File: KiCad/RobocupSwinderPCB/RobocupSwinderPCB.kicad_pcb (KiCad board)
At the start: 2 copper layers, 92 x 57 mm, 30 parts, among them J1 Barrel_Jack, M1 Stepper_Motor_bipolar, M2 Stepper_Motor_bipolar, SW1 Limit_Switch, SW2 Limit_Switch, SW3 SW_SPST, U1 Teensy4.1, U3 LM7805_TO220

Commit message: Pcb cleanup
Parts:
- U1: footprint TeensyLibrary:Teensy41-Pins-Only_Silkscreen -> SwinderFootprintLibrary:Teensy41-Pins-Only_Silkscreen
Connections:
- LCD1 pad 3: /LCD_SDA_Pin_18 -> /LCD_SCL_Pin_19
- LCD1 pad 4: /LCD_SCL_Pin_19 -> /LCD_SDA_Pin_18
- RE1 pad 3: /RE_SW_Pin_21 -> /RE_CLK_Pin_23
- RE1 pad 5: /RE_CLK_Pin_23 -> /RE_SW_Pin_21
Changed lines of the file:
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@@
 		)
 		(property ki_fp_filters "SW*DPDT*")
-		(sheetname "Root")
+		(sheetname "/")
 		(sheetfile "RobocupSwinderPCB.kicad_sch")
 		(attr through_hole)
@@
 		)
 		(property ki_fp_filters "R_*")
-		(sheetname "Root")
+		(sheetname "/")
 		(sheetfile "RobocupSwinderPCB.kicad_sch")
 		(attr smd)
@@
 		)
 		(property ki_fp_filters "CP_*")
-		(sheetname "Root")
+		(sheetname "/")
 		(sheetfile "RobocupSwinderPCB.kicad_sch")
 		(attr through_hole)
@@
 		)
 		(property ki_fp_filters "SW*DPDT*")
-		(sheetname "Root")
+		(sheetname "/")
 		(sheetfile "RobocupSwinderPCB.kicad_sch")
 		(attr through_hole)
@@
 		)
 		(property ki_fp_filters "LED* LED_SMD:* LED_THT:*")
-		(sheetname "Root")
+		(sheetname "/")
 		(sheetfile "RobocupSwinderPCB.kicad_sch")
 		(attr smd)
@@
 		)
 		(property ki_fp_filters "MountingHole*Pad*")
-		(sheetname "Root")
+		(sheetname "/")
 		(sheetfile "RobocupSwinderPCB.kicad_sch")
 		(attr exclude_from_pos_files exclude_from_bom)
@@
 		)
 		(property ki_fp_filters "R_*")
-		(sheetname "Root")
+		(sheetname "/")
 		(sheetfile "RobocupSwinderPCB.kicad_sch")
 		(attr smd)
@@
 			)
 		)
-		(sheetname "Root")
+		(sheetname "/")
 		(sheetfile "RobocupSwinderPCB.kicad_sch")
 		(attr through_hole)
@@
 			(layers "*.Cu" "*.Mask")
 			(remove_unused_layers no)
-			(net 25 "/LCD_SDA_Pin_18")
+			(net 26 "/LCD_SCL_Pin_19")
 			(pinfunction "SDA")
 			(pintype "bidirectional")
@@
 			(layers "*.Cu" "*.Mask")
 			(remove_unused_layers no)
-			(net 26 "/LCD_SCL_Pin_19")
+			(net 25 "/LCD_SDA_Pin_18")
 			(pinfunction "SCL")
 			(pintype "bidirectional")
@@
 		)
 		(property ki_fp_filters "MountingHole*Pad*")
-		(sheetname "Root")
+		(sheetname "/")
 		(sheetfile "RobocupSwinderPCB.kicad_sch")
 		(attr exclude_from_pos_files exclude_from_bom)
@@
 			)
 		)
-		(sheetname "Root")
+		(sheetname "/")
 		(sheetfile "RobocupSwinderPCB.kicad_sch")
 		(attr through_hole)
@@
 		)
 	)
-	(footprint "TeensyLibrary:Teensy41-Pins-Only_Silkscreen"
+	(footprint "SwinderFootprintLibrary:Teensy41-Pins-Only_Silkscreen"
 		(layer "F.Cu")
 		(at 133.01 104.37)
 		(property "Reference" "U1"
-			(at 0.07 9.98 0)
+			(at 0 -10.16 0)
 			(layer "F.SilkS")
 			(effects
@@
 			)
 		)
-		(sheetname "Root")
+		(sheetname "/")
 		(sheetfile "RobocupSwinderPCB.kicad_sch")
 		(attr through_hole)
@@
 			(effects
 				(font
-					(size 0.8 0.8)
+					(size 0.7 0.7)
 					(thickness 0.15)
 				)
@@
 			(effects
 				(font
-					(size 0.8 0.8)
+					(size 0.7 0.7)
 					(thickness 0.15)
 				)
@@
 		)
 		(property ki_fp_filters "Pololu*Breakout*15.2x20.3mm*")
-		(sheetname "Root")
+		(sheetname "/")
 		(sheetfile "RobocupSwinderPCB.kicad_sch")
 		(attr through_hole)
@@
 		)
 		(property ki_fp_filters "BarrelJack*")
-		(sheetname "Root")
+		(sheetname "/")
 		(sheetfile "RobocupSwinderPCB.kicad_sch")
 		(attr through_hole)
@@
 		)
 		(property ki_fp_filters "Choke_* *Coil* Inductor_* L_*")
-		(sheetname "Root")
+		(sheetname "/")
 		(sheetfile "RobocupSwinderPCB.kicad_sch")
 		(attr smd)
@@
 		)
 		(property ki_fp_filters "PinHeader*P2.54mm*Vertical* TerminalBlock* Motor*")
-		(sheetname "Root")
+		(sheetname "/")
 		(sheetfile "RobocupSwinderPCB.kicad_sch")
 		(attr through_hole)
@@
 		)
 		(property ki_fp_filters "C_*")
-		(sheetname "Root")
+		(sheetname "/")
 		(sheetfile "RobocupSwinderPCB.kicad_sch")
 		(attr smd)
@@
 		)
 		(property ki_fp_filters "TO?220*")
-		(sheetname "Root")
+		(sheetname "/")
 		(sheetfile "RobocupSwinderPCB.kicad_sch")
 		(attr smd)
@@
 		)
 		(property ki_fp_filters "MountingHole*Pad*")
-		(sheetname "Root")
+		(sheetname "/")
 		(sheetfile "RobocupSwinderPCB.kicad_sch")
 		(attr exclude_from_pos_files exclude_from_bom)
@@
 		)
 		(property ki_fp_filters "CP_*")
-		(sheetname "Root")
+		(sheetname "/")
 		(sheetfile "RobocupSwinderPCB.kicad_sch")
 		(attr through_hole)
@@
 		)
 		(property ki_fp_filters "PinHeader*P2.54mm*Vertical* TerminalBlock* Motor*")
-		(sheetname "Root")
+		(sheetname "/")
 		(sheetfile "RobocupSwinderPCB.kicad_sch")
 		(attr through_hole)
@@
 			)
 		)
-		(sheetname "Root")
+		(sheetname "/")
 		(sheetfile "RobocupSwinderPCB.kicad_sch")
 		(attr through_hole)
@@
 			(layers "*.Cu" "*.Mask")
 			(remove_unused_layers no)
-			(net 29 "/RE_SW_Pin_21")
+			(net 31 "/RE_CLK_Pin_23")
 			(pinfunction "CLK")
 			(pintype "output")
@@
 			(layers "*.Cu" "*.Mask")
 			(remove_unused_layers no)
-			(net 31 "/RE_CLK_Pin_23")
+			(net 29 "/RE_SW_Pin_21")
 			(pinfunction "SW")
 			(pintype "output")
@@
 		)
 		(property ki_fp_filters "R_*")
-		(sheetname "Root")
+		(sheetname "/")
 		(sheetfile "RobocupSwinderPCB.kicad_sch")
 		(attr smd)
@@
 		)
 		(property ki_fp_filters "C_*")
-		(sheetname "Root")
+		(sheetname "/")
 		(sheetfile "RobocupSwinderPCB.kicad_sch")
 		(attr smd)
@@
 		)
 		(property ki_fp_filters "*Fuse*")
-		(sheetname "Root")
+		(sheetname "/")
 		(sheetfile "RobocupSwinderPCB.kicad_sch")
 		(attr smd)
@@
 		)
 		(property ki_fp_filters "C_*")
-		(sheetname "Root")
+		(sheetname "/")
 		(sheetfile "RobocupSwinderPCB.kicad_sch")
 		(attr smd)
@@
 		)
 		(property ki_fp_filters "R_*")
-		(sheetname "Root")
+		(sheetname "/")
 		(sheetfile "RobocupSwinderPCB.kicad_sch")
 		(attr smd)
@@
 		)
 		(property ki_fp_filters "LED* LED_SMD:* LED_THT:*")
-		(sheetname "Root")
+		(sheetname "/")
 		(sheetfile "RobocupSwinderPCB.kicad_sch")
 		(attr smd)
@@
 		)
 		(property ki_fp_filters "Pololu*Breakout*15.2x20.3mm*")
-		(sheetname "Root")
+		(sheetname "/")
 		(sheetfile "RobocupSwinderPCB.kicad_sch")
 		(attr through_hole)
@@
 		)
 		(property ki_fp_filters "MountingHole*Pad*")
-		(sheetname "Root")
+		(sheetname "/")
 		(sheetfile "RobocupSwinderPCB.kicad_sch")
 		(attr exclude_from_pos_files exclude_from_bom)

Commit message: More pcb cleanup.
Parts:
- G***: footprint Library:RoboBuzz -> SwinderFootprintLibrary:RoboBuzz
- J1: footprint Library:CUI_PJ-037A -> SwinderFootprintLibrary:CUI_PJ-037A
- moved J1 0.40 mm to (106.2, 76.4)
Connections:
- net Net-(SW3-A) renamed /PWR_SW_IN
- net Net-(SW3-B) renamed /PWR_SW_OUT
- LCD1 pad 3: /LCD_SCL_Pin_19 -> /LCD_SDA_Pin_18
- LCD1 pad 4: /LCD_SDA_Pin_18 -> /LCD_SCL_Pin_19
- RE1 pad 3: /RE_CLK_Pin_23 -> /RE_CLK_Pin_21
- RE1 pad 5: /RE_SW_Pin_21 -> /RE_SW_Pin_23
- U1 pad 43: /RE_SW_Pin_21 -> /RE_CLK_Pin_21
- U1 pad 45: /RE_CLK_Pin_23 -> /RE_SW_Pin_23
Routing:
- net /RE_SW_Pin_23: track 0.00 -> 75.2 mm
- net /RE_CLK_Pin_23: track 75.2 -> 0.00 mm
- net /RE_SW_Pin_21: track 70.5 -> 0.00 mm
- net /RE_CLK_Pin_21: track 0.00 -> 70.5 mm

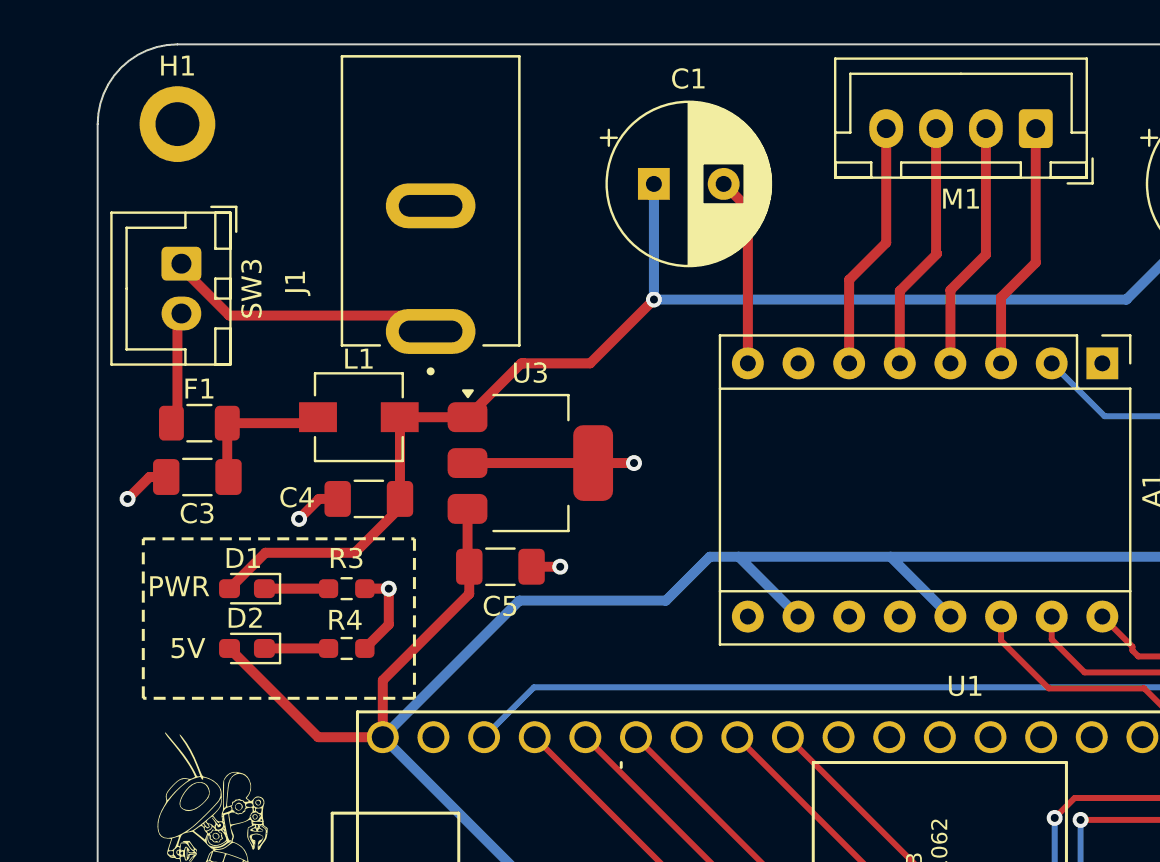
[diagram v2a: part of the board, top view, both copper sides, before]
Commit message: Removed filter inductor and cap.
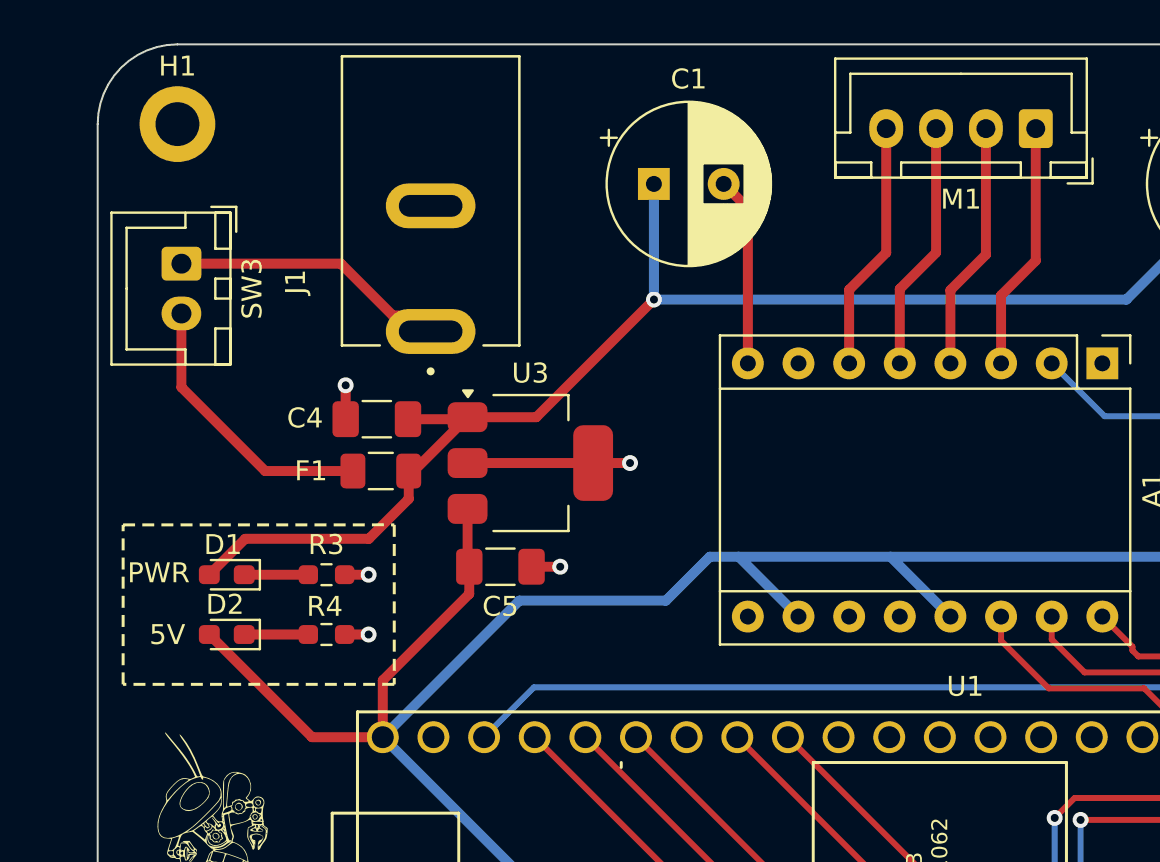
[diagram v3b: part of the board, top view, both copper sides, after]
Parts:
- removed C3: 10uF, Capacitor_SMD:C_1206_3216Metric_Pad1.33x1.80mm_HandSolder
- removed L1: 5.6uH, Inductor_SMD:L_TracoPower_TCK-141
- C4: value 10uF -> 0.22uF
- moved F1 9.41 mm to (103.7, 83.4)
- moved C4 4.02 mm to (103.5, 80.8)
- moved D1 1.23 mm to (96.0, 88.6)
- moved D2 1.23 mm to (96.0, 91.6)
- moved R3 1.23 mm to (101.0, 88.6)
- moved R4 1.23 mm to (101.0, 91.6)
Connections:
- F1 pad 2: Net-(C3-Pad1) -> VCC
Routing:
- net /PWR_SW_OUT: track 5.62 -> 14.0 mm
- net Net-(C3-Pad1): track 7.40 -> 0.00 mm
- net GND: track 19.2 -> 13.7 mm
- net VCC: track 67.2 -> 69.1 mm
- net +5V: track 156.7 -> 158.0 mm

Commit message: fixed pin name.
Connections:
- net /Coil_FLT_Pin_22 renamed /Coil_FLT_Pin_30
- net /Feed_FLT_Pin_21 renamed /Feed_FLT_Pin_29
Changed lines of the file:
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@@
 	(net 7 "/Feed_SLP_Pin_40")
 	(net 8 "Net-(A1-B2)")
-	(net 9 "/Feed_FLT_Pin_21")
+	(net 9 "/Feed_FLT_Pin_29")
 	(net 10 "+5V")
 	(net 11 "unconnected-(A2-~{EN}-Pad9)")
-	(net 12 "/Coil_FLT_Pin_22")
+	(net 12 "/Coil_FLT_Pin_30")
 	(net 13 "Net-(A2-A2)")
 	(net 14 "Net-(A2-A1)")
@@
 			(layers "*.Cu" "*.Mask")
 			(remove_unused_layers no)
-			(net 9 "/Feed_FLT_Pin_21")
+			(net 9 "/Feed_FLT_Pin_29")
 			(pinfunction "29_TX7")
 			(pintype "bidirectional")
@@
 			(layers "*.Cu" "*.Mask")
 			(remove_unused_layers no)
-			(net 12 "/Coil_FLT_Pin_22")
+			(net 12 "/Coil_FLT_Pin_30")
 			(pinfunction "30_CRX3")
 			(pintype "bidirectional")
@@
 			(layers "*.Cu" "*.Mask")
 			(remove_unused_layers no)
-			(net 12 "/Coil_FLT_Pin_22")
+			(net 12 "/Coil_FLT_Pin_30")
 			(pinfunction "~{FLT}")
 			(pintype "output")
@@
 			(layers "*.Cu" "*.Mask")
 			(remove_unused_layers no)
-			(net 9 "/Feed_FLT_Pin_21")
+			(net 9 "/Feed_FLT_Pin_29")
 			(pinfunction "~{FLT}")
 			(pintype "output")
